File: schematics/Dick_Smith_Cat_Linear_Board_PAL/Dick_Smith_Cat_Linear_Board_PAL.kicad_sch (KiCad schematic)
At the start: 40 parts, among them J1 Motherboard, Q5 1402D, Q8 1702M, SW1 RESET, SW900 Color Defeat, U47 74LS00, U48 TEA 1002

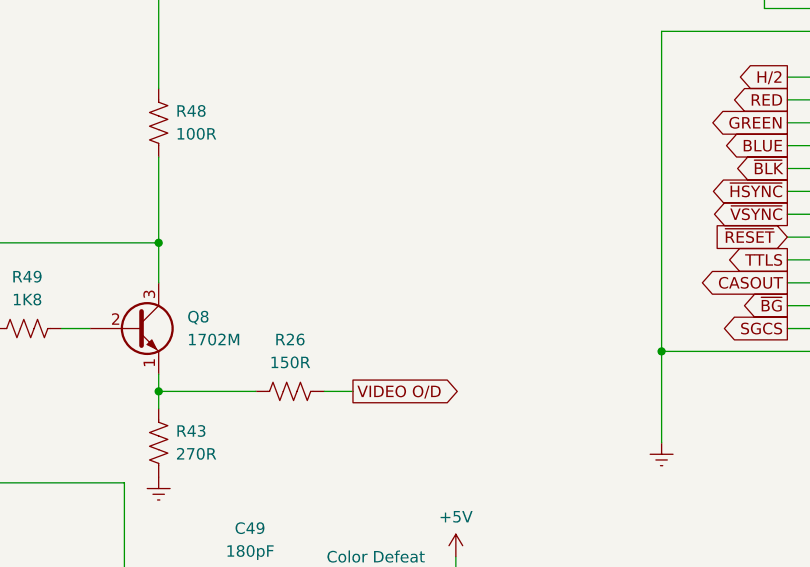
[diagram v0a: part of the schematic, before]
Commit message: Add pinout for composite video connector on linear board
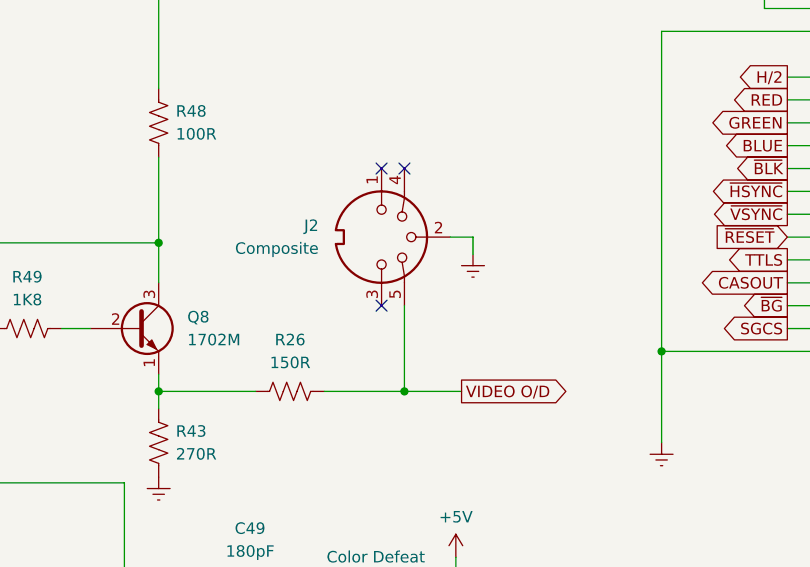
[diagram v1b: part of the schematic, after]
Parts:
- added J2: Composite, symbol Connector:DIN-5_180degree
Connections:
- net Earth: now also J2.2
- net VIDEO O/D: now also J2.5
- no-connect marks 4 -> 7
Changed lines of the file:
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@@
   (junction (at 146.685 74.295) (diameter 0) (color 0 0 0 0)
   )
+  (junction (at 206.375 78.105) (diameter 0) (color 0 0 0 0)
+  )
+  (no_connect (at 203.835 53.34))
   (no_connect (at 255.905 78.74))
   (no_connect (at 255.905 30.48))
+  (no_connect (at 203.835 68.58))
+  (no_connect (at 206.375 53.34))
   (no_connect (at 86.36 83.185))
   (no_connect (at 255.905 76.2))
@@
     (stroke (width 0) (type default))
   )
+  (wire (pts (xy 206.375 78.105) (xy 212.725 78.105))
+    (stroke (width 0) (type default))
+  )
   (wire (pts (xy 86.36 88.265) (xy 83.185 88.265))
     (stroke (width 0) (type default))
@@
     (stroke (width 0) (type default))
   )
-  (wire (pts (xy 197.485 78.105) (xy 200.66 78.105))
+  (wire (pts (xy 197.485 78.105) (xy 206.375 78.105))
     (stroke (width 0) (type default))
   )
@@
     (stroke (width 0) (type default))
   )
+  (wire (pts (xy 213.995 60.96) (xy 213.995 62.865))
+    (stroke (width 0) (type default))
+  )
   (wire (pts (xy 142.24 104.14) (xy 152.4 104.14))
     (stroke (width 0) (type default))
@@
   )
   (wire (pts (xy 252.73 40.64) (xy 255.905 40.64))
+    (stroke (width 0) (type default))
+  )
+  (wire (pts (xy 206.375 68.58) (xy 206.375 78.105))
     (stroke (width 0) (type default))
   )
@@
   )
   (wire (pts (xy 54.61 126.365) (xy 54.61 121.285))
+    (stroke (width 0) (type default))
+  )
+  (wire (pts (xy 211.455 60.96) (xy 213.995 60.96))
     (stroke (width 0) (type default))
   )
@@
     )
   )
-  (global_label "VIDEO O{slash}D" (shape output) (at 200.66 78.105 0) (fields_autoplaced)
+  (global_label "VIDEO O{slash}D" (shape output) (at 212.725 78.105 0) (fields_autoplaced)
     (effects (font (size 1.27 1.27)) (justify left))
-    (property "Intersheetrefs" "${INTERSHEET_REFS}" (at 213.9867 78.105 0)
+    (property "Intersheetrefs" "${INTERSHEET_REFS}" (at 226.0517 78.105 0)
       (effects (font (size 1.27 1.27)) (justify left) hide)
     )
@@
     )
   )
+  (symbol (lib_id "Connector:DIN-5_180degree") (at 203.835 60.96 270) (unit 1)
+    (in_bom yes) (on_board yes) (dnp no) (fields_autoplaced)
+    (property "Reference" "J2" (at 196.85 59.6901 90)
+      (effects (font (size 1.27 1.27)) (justify right))
+    )
+    (property "Value" "Composite" (at 196.85 62.2301 90)
+      (effects (font (size 1.27 1.27)) (justify right))
+    )
+    (property "Footprint" "" (at 203.835 60.96 0)
+      (effects (font (size 1.27 1.27)) hide)
+    )
+    (property "Datasheet" "http://www.mouser.com/ds/2/18/40_c091_abd_e-75918.pdf" (at 203.835 60.96 0)
+      (effects (font (size 1.27 1.27)) hide)
+    )
+    (pin "1")
+    (pin "5")
+    (pin "3")
+    (pin "2")
+    (pin "4")
+    (instances
+      (project "Dick_Smith_Cat_Linear_Board_PAL"
+        (path "/cc76f27d-e855-48d8-b206-3df41b400bec"
+          (reference "J2") (unit 1)
+        )
+      )
+    )
+  )
   (symbol (lib_id "Device:C_Trim") (at 110.49 61.595 0) (unit 1)
     (in_bom yes) (on_board yes) (dnp no) (fields_autoplaced)
@@
         )
       )
+    )
+  )
+  (symbol (lib_id "power:Earth") (at 213.995 62.865 0) (unit 1)
+    (in_bom yes) (on_board yes) (dnp no) (fields_autoplaced)
+    (property "Reference" "#PWR047" (at 213.995 69.215 0)
+      (effects (font (size 1.27 1.27)) hide)
+    )
+    (property "Value" "Earth" (at 213.995 66.675 0)
+      (effects (font (size 1.27 1.27)) hide)
+    )
+    (property "Footprint" "" (at 213.995 62.865 0)
+      (effects (font (size 1.27 1.27)) hide)
+    )
+    (property "Datasheet" "~" (at 213.995 62.865 0)
+      (effects (font (size 1.27 1.27)) hide)
+    )
+    (pin "1")
+    (instances
+      (project "Dick_Smith_Cat_Linear_Board_PAL"
+        (path "/cc76f27d-e855-48d8-b206-3df41b400bec"
+          (reference "#PWR047") (unit 1)
+        )
+      )

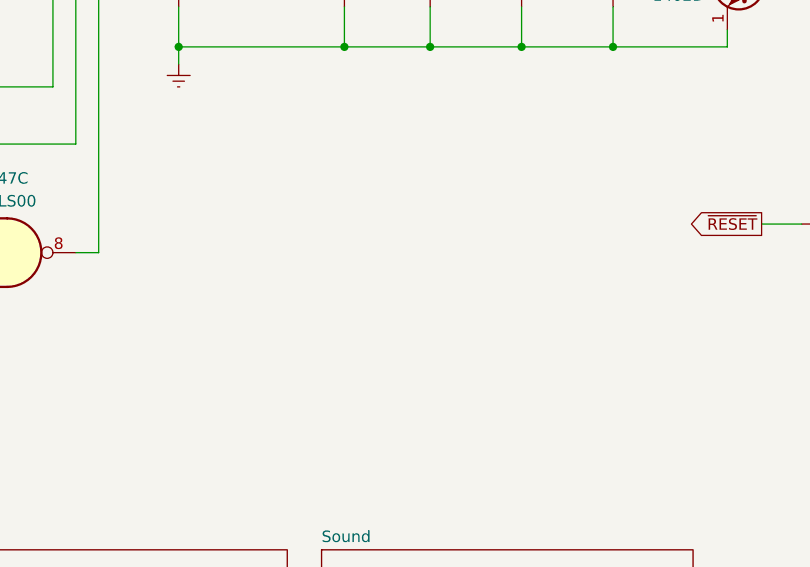
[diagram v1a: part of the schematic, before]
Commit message: Add more connector pinouts to the schematics
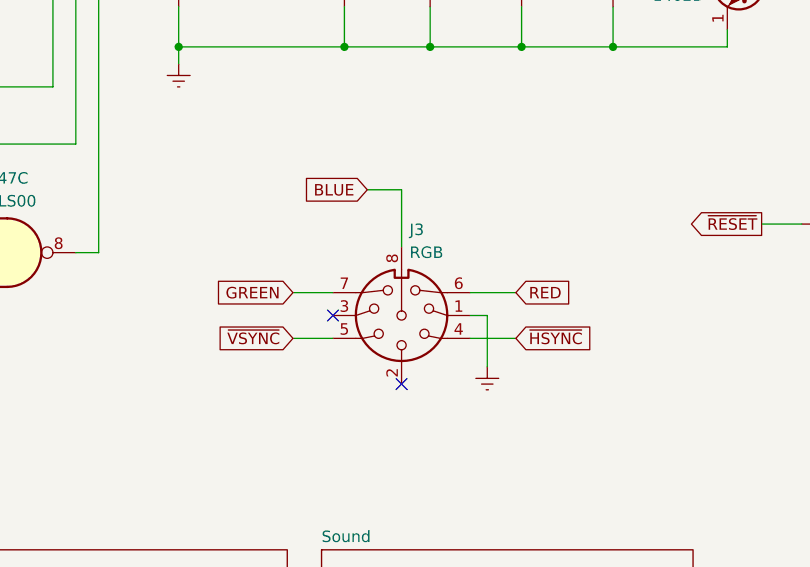
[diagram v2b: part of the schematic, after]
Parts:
- added J3: RGB, symbol Connector:DIN-8
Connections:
- net BLUE: now also J3.8
- net Earth: now also J3.1
- net GREEN: now also J3.7
- net RED: now also J3.6
- net ~{HSYNC}: now also J3.4
- net ~{VSYNC}: now also J3.5
- no-connect marks 7 -> 9
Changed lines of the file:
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@@
   (no_connect (at 203.835 53.34))
   (no_connect (at 255.905 78.74))
+  (no_connect (at 139.065 156.845))
   (no_connect (at 255.905 30.48))
+  (no_connect (at 131.445 149.225))
   (no_connect (at 203.835 68.58))
   (no_connect (at 206.375 53.34))
@@
     (stroke (width 0) (type default))
   )
+  (wire (pts (xy 139.065 135.255) (xy 139.065 141.605))
+    (stroke (width 0) (type default))
+  )
   (wire (pts (xy 206.375 78.105) (xy 212.725 78.105))
     (stroke (width 0) (type default))
@@
     (stroke (width 0) (type default))
   )
+  (wire (pts (xy 146.685 149.225) (xy 148.59 149.225))
+    (stroke (width 0) (type default))
+  )
   (wire (pts (xy 134.62 74.295) (xy 136.525 74.295))
     (stroke (width 0) (type default))
@@
     (stroke (width 0) (type default))
   )
+  (wire (pts (xy 146.685 146.685) (xy 151.765 146.685))
+    (stroke (width 0) (type default))
+  )
   (wire (pts (xy 97.79 113.03) (xy 97.79 97.155))
     (stroke (width 0) (type default))
@@
     (stroke (width 0) (type default))
   )
+  (wire (pts (xy 135.255 135.255) (xy 139.065 135.255))
+    (stroke (width 0) (type default))
+  )
   (wire (pts (xy 39.37 76.835) (xy 71.755 76.835))
     (stroke (width 0) (type default))
@@
     (stroke (width 0) (type default))
   )
+  (wire (pts (xy 146.685 151.765) (xy 151.765 151.765))
+    (stroke (width 0) (type default))
+  )
   (wire (pts (xy 45.085 31.115) (xy 45.085 33.02))
     (stroke (width 0) (type default))
@@
     (stroke (width 0) (type default))
   )
+  (wire (pts (xy 127 146.685) (xy 131.445 146.685))
+    (stroke (width 0) (type default))
+  )
   (wire (pts (xy 51.435 41.91) (xy 51.435 43.18))
     (stroke (width 0) (type default))
@@
     (stroke (width 0) (type default))
   )
+  (wire (pts (xy 127 151.765) (xy 131.445 151.765))
+    (stroke (width 0) (type default))
+  )
   (wire (pts (xy 63.5 41.91) (xy 63.5 43.18))
     (stroke (width 0) (type default))
@@
   )
   (wire (pts (xy 44.45 71.755) (xy 86.36 71.755))
+    (stroke (width 0) (type default))
+  )
+  (wire (pts (xy 148.59 149.225) (xy 148.59 154.94))
     (stroke (width 0) (type default))
   )
@@
     )
   )
+  (global_label "~{HSYNC}" (shape input) (at 151.765 151.765 0) (fields_autoplaced)
+    (effects (font (size 1.27 1.27)) (justify left))
+    (property "Intersheetrefs" "${INTERSHEET_REFS}" (at 160.9793 151.765 0)
+      (effects (font (size 1.27 1.27)) (justify left) hide)
+    )
+  )
   (global_label "~{BG}" (shape input) (at 39.37 110.49 180) (fields_autoplaced)
     (effects (font (size 1.27 1.27)) (justify right))
@@
     )
   )
+  (global_label "RED" (shape input) (at 151.765 146.685 0) (fields_autoplaced)
+    (effects (font (size 1.27 1.27)) (justify left))
+    (property "Intersheetrefs" "${INTERSHEET_REFS}" (at 158.4392 146.685 0)
+      (effects (font (size 1.27 1.27)) (justify left) hide)
+    )
+  )
   (global_label "~{VSYNC}" (shape input) (at 39.37 144.78 180) (fields_autoplaced)
     (effects (font (size 1.27 1.27)) (justify right))
@@
     )
   )
+  (global_label "GREEN" (shape input) (at 127 146.685 180) (fields_autoplaced)
+    (effects (font (size 1.27 1.27)) (justify right))
+    (property "Intersheetrefs" "${INTERSHEET_REFS}" (at 117.8463 146.685 0)
+      (effects (font (size 1.27 1.27)) (justify right) hide)
+    )
+  )
   (global_label "RED" (shape input) (at 39.37 71.755 180) (fields_autoplaced)
     (effects (font (size 1.27 1.27)) (justify right))
@@
     )
   )
+  (global_label "~{VSYNC}" (shape input) (at 127 151.765 180) (fields_autoplaced)
+    (effects (font (size 1.27 1.27)) (justify right))
+    (property "Intersheetrefs" "${INTERSHEET_REFS}" (at 118.0276 151.765 0)
+      (effects (font (size 1.27 1.27)) (justify right) hide)
+    )
+  )
   (global_label "BLUE" (shape output) (at 248.92 50.8 180) (fields_autoplaced)
     (effects (font (size 1.27 1.27)) (justify right))
@@
     (effects (font (size 1.27 1.27)) (justify right))
     (property "Intersheetrefs" "${INTERSHEET_REFS}" (at 230.2714 33.02 0)
+      (effects (font (size 1.27 1.27)) (justify right) hide)
+    )
+  )
+  (global_label "BLUE" (shape input) (at 135.255 135.255 180) (fields_autoplaced)
+    (effects (font (size 1.27 1.27)) (justify right))
+    (property "Intersheetrefs" "${INTERSHEET_REFS}" (at 127.4922 135.255 0)
       (effects (font (size 1.27 1.27)) (justify right) hide)
     )
@@
     )
   )
+  (symbol (lib_id "Connector:DIN-8") (at 139.065 149.225 180) (unit 1)
+    (in_bom yes) (on_board yes) (dnp no) (fields_autoplaced)
+    (property "Reference" "J3" (at 139.9539 139.7 0)
+      (effects (font (size 1.27 1.27)) (justify right))
+    )
+    (property "Value" "RGB" (at 139.9539 142.24 0)
+      (effects (font (size 1.27 1.27)) (justify right))
+    )
+    (property "Footprint" "" (at 139.065 149.225 0)
+      (effects (font (size 1.27 1.27)) hide)
+    )
+    (property "Datasheet" "http://www.mouser.com/ds/2/18/40_c091_abd_e-75918.pdf" (at 139.065 149.225 0)
+      (effects (font (size 1.27 1.27)) hide)
+    )
+    (pin "8")
+    (pin "1")
+    (pin "6")
+    (pin "5")
+    (pin "4")
+    (pin "3")
+    (pin "7")
+    (pin "2")
+    (instances
+      (project "Dick_Smith_Cat_Linear_Board_PAL"
+        (path "/cc76f27d-e855-48d8-b206-3df41b400bec"
+          (reference "J3") (unit 1)
+        )
+      )
+    )
+  )
   (symbol (lib_id "power:+5V") (at 26.035 165.735 0) (unit 1)
     (in_bom yes) (on_board yes) (dnp no) (fields_autoplaced)
@@
         )
       )
+    )
+  )
+  (symbol (lib_id "power:Earth") (at 148.59 154.94 0) (unit 1)
+    (in_bom yes) (on_board yes) (dnp no) (fields_autoplaced)
+    (property "Reference" "#PWR048" (at 148.59 161.29 0)
+      (effects (font (size 1.27 1.27)) hide)
+    )
+    (property "Value" "Earth" (at 148.59 158.75 0)
+      (effects (font (size 1.27 1.27)) hide)
+    )
+    (property "Footprint" "" (at 148.59 154.94 0)
+      (effects (font (size 1.27 1.27)) hide)
+    )
+    (property "Datasheet" "~" (at 148.59 154.94 0)
+      (effects (font (size 1.27 1.27)) hide)
+    )
+    (pin "1")
+    (instances
+      (project "Dick_Smith_Cat_Linear_Board_PAL"
+        (path "/cc76f27d-e855-48d8-b206-3df41b400bec"
+          (reference "#PWR048") (unit 1)
+        )
+      )
